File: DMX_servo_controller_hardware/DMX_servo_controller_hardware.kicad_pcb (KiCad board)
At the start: 4 copper layers, 100 x 100 mm, 61 parts, among them J1 To_XLR3, J2 To_XLR3, J3 Power connector, J4 Display, J5 Rotary encoder, J6 Output block 1, J7 Output block 2, J8 Output block 3, J9 Output block 4, Q1 BSS138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

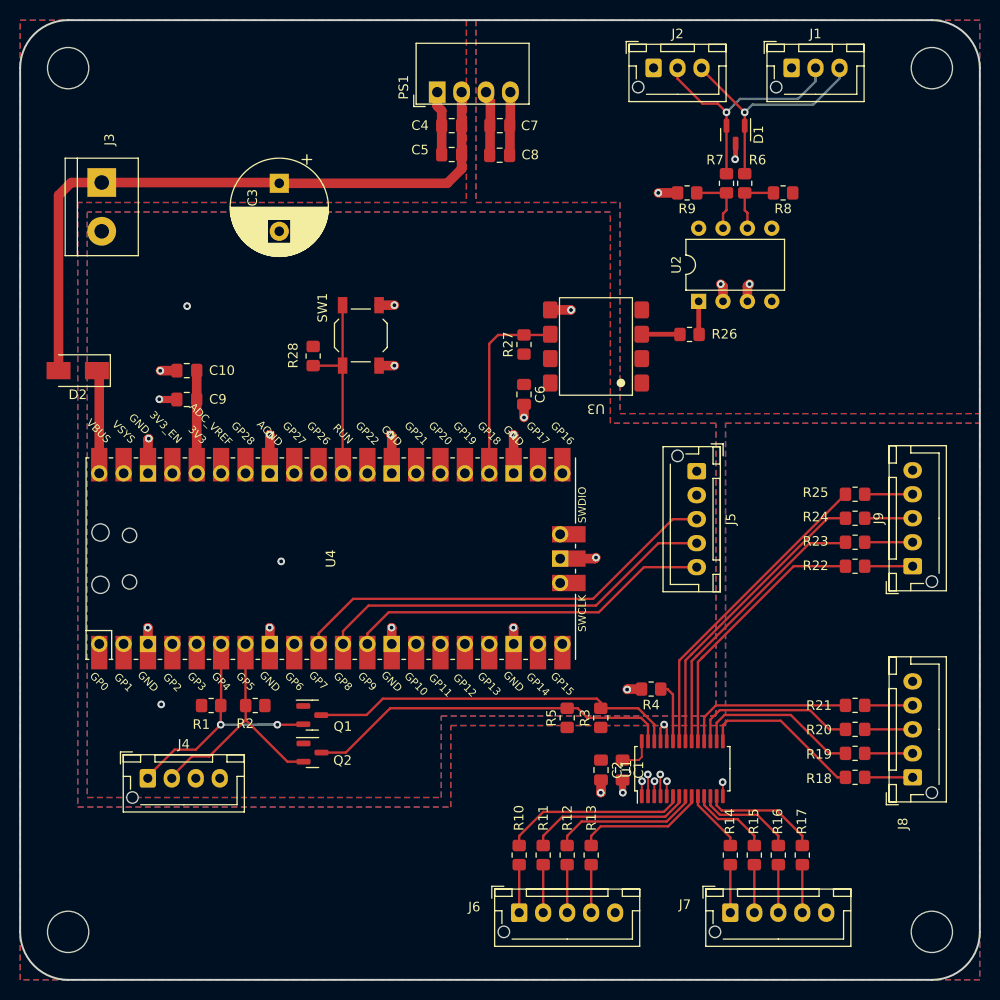
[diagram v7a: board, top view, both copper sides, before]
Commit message: Reorganizes component positioning/layout
The connectors are now all close to the edge o the board and grouped by
function.

The space between components in the DMX and uC sections was reduced,
leaving some space to reduce the overall board size later a bit if we
decide to.
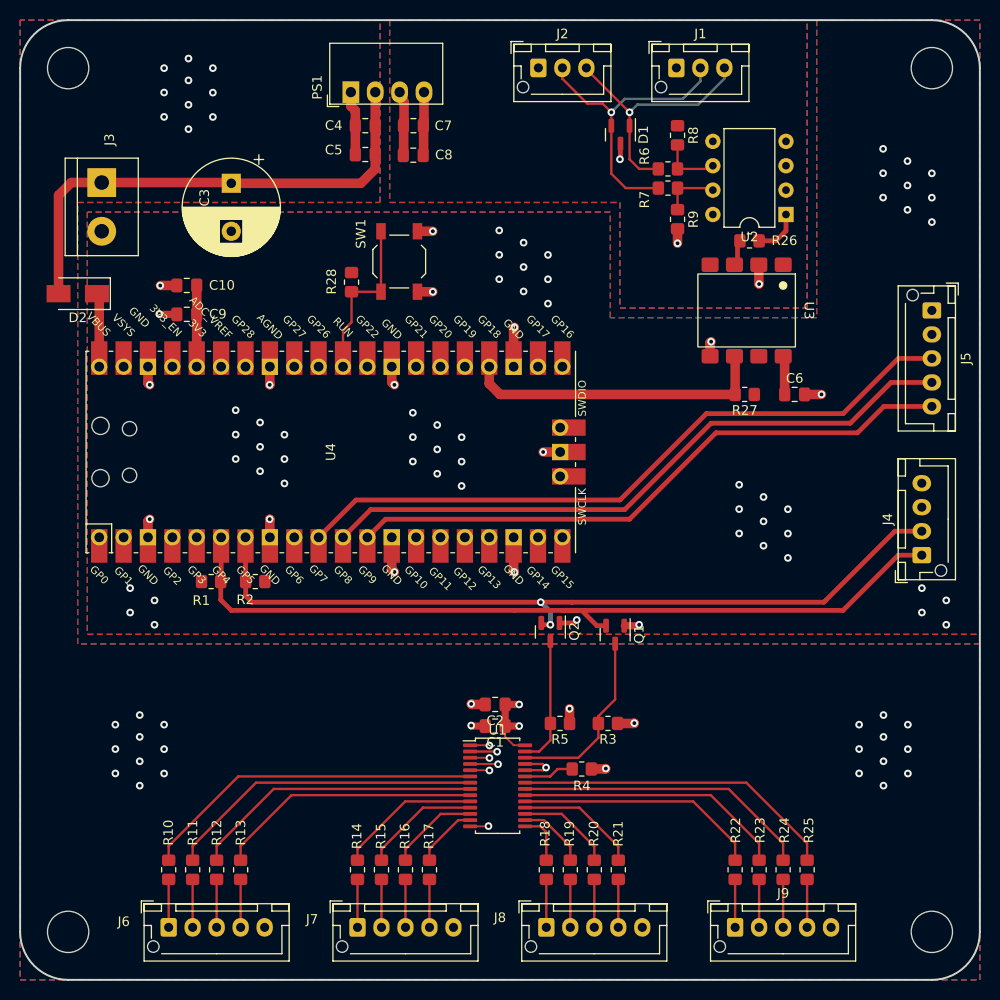
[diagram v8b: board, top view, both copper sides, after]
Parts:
- moved J4 83.9 mm to (193.9, 115.8), turned to 90 degrees
- moved J9 41.9 mm to (174.5, 154.5), turned to 0 degrees
- moved J8 41.3 mm to (154.8, 154.5), turned to 0 degrees
- moved R25 39.4 mm to (182.0, 148.5), turned to -90 degrees
- moved J7 38.9 mm to (135.2, 154.5)
- moved R14 38.9 mm to (135.2, 148.5)
- moved R15 38.9 mm to (137.7, 148.5)
- moved R16 38.9 mm to (140.2, 148.5)
- moved R17 38.9 mm to (142.7, 148.5)
- moved R24 37.4 mm to (179.5, 148.5), turned to -90 degrees
- moved J6 36.6 mm to (115.5, 154.5)
- moved R10 36.6 mm to (115.5, 148.5)
- moved R11 36.6 mm to (118.0, 148.5)
- moved R12 36.6 mm to (120.5, 148.5)
- moved R13 36.6 mm to (123.0, 148.5)
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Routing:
- net I2C0_SDA: track 29.2 -> 87.8 mm, vias 2 -> 0
- net I2C0_SCL: track 26.1 -> 83.5 mm, vias 0 -> 2
- net Encoder CLK: track 38.3 -> 64.5 mm
- net Encoder SW: track 45.4 -> 71.6 mm
- net Encoder DT: track 42.0 -> 68.0 mm
- net Net-(Q2-D): track 38.4 -> 13.5 mm
- net Net-(Q1-D): track 38.6 -> 19.0 mm
- net Net-(U1-LED0): track 19.1 -> 35.9 mm
- net Net-(U1-LED1): track 17.3 -> 33.1 mm
- net Net-(U1-LED2): track 15.4 -> 30.4 mm
- net Net-(U1-LED3): track 13.6 -> 27.6 mm
- net Net-(U1-LED8): track 17.1 -> 5.39 mm
- net DMX_signal: track 20.3 -> 31.9 mm
- net Net-(U1-LED9): track 17.3 -> 7.28 mm
- net +5V: track 73.2 -> 64.5 mm, vias 0 -> 34
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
